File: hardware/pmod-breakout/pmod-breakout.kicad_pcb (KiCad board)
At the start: 2 copper layers, 50 x 22.9 mm, 3 parts, among them J1 Feather, J2 PMOD, J3 PMOD

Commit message: updated board + pmod
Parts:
- added REF**: Josh Details, josh-footprints:JoshDetails, B.Cu at (111.8, 65.3)
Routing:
- added copper zone on F.Cu, net GND
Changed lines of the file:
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@@
     (tracks 79)
     (zones 0)
-    (modules 3)
+    (modules 4)
     (nets 19)
   )
@@
     (last_trace_width 0.25)
     (trace_clearance 0.2)
-    (zone_clearance 0.508)
+    (zone_clearance 0.2)
     (zone_45_only no)
     (trace_min 0.2)
@@
     (solder_mask_min_width 0.25)
     (aux_axis_origin 0 0)
-    (visible_elements FFFFFF7F)
+    (visible_elements 7FFFFFFF)
     (pcbplotparams
       (layerselection 0x010fc_ffffffff)
@@
     (add_net /P2_9)
     (add_net GND)
-    (add_net "Net-(J1-Pad1)")
-    (add_net "Net-(J1-Pad13)")
-    (add_net "Net-(J1-Pad14)")
-    (add_net "Net-(J1-Pad15)")
-    (add_net "Net-(J1-Pad25)")
-    (add_net "Net-(J1-Pad26)")
-    (add_net "Net-(J1-Pad27)")
-    (add_net "Net-(J1-Pad28)")
-    (add_net "Net-(J1-Pad3)")
+  )
+  (module josh-footprints:JoshDetails (layer B.Cu)
+    (at 111.78 65.35 180)
+    (fp_text reference REF** (at 0 5.6) (layer B.Fab)
+      (effects (font (size 1 1) (thickness 0.15)) (justify mirror))
+    )
+    (fp_text value "Josh Details" (at 0 6.6) (layer B.Fab)
+      (effects (font (size 1 1) (thickness 0.15)) (justify mirror))
+    )
+    (fp_text user github.com/joshajohnson/iCE40-fpga (at 9.69 -2.19) (layer B.SilkS)
+      (effects (font (size 1 1) (thickness 0.15)) (justify mirror))
+    )
+    (fp_text user joshajohnson.com (at 2 -0.5) (layer B.SilkS)
+      (effects (font (size 1 1) (thickness 0.15)) (justify mirror))
+    )
+    (fp_text user "Josh Johnson" (at 0.2 1 180) (layer B.SilkS)
+      (effects (font (size 1 1) (thickness 0.15)) (justify mirror))
+    )
   )
   (module josh-footprints:PMOD_HOST locked (layer F.Cu)
@@
       )
     )
+  )
+  (zone (net 2) (net_name GND) (layer F.Cu) (hatch edge 0.508)
+    (connect_pads (clearance 0.2))
+    (min_thickness 0.2)
+    (fill yes (arc_segments 32) (thermal_gap 0.21) (thermal_bridge_width 0.21))
+    (polygon
+      (pts
+        (xy 85.66 57.36) (xy 135.885 57.321986) (xy 135.935 80.398013) (xy 85.71 80.436027)
+      )
+    )

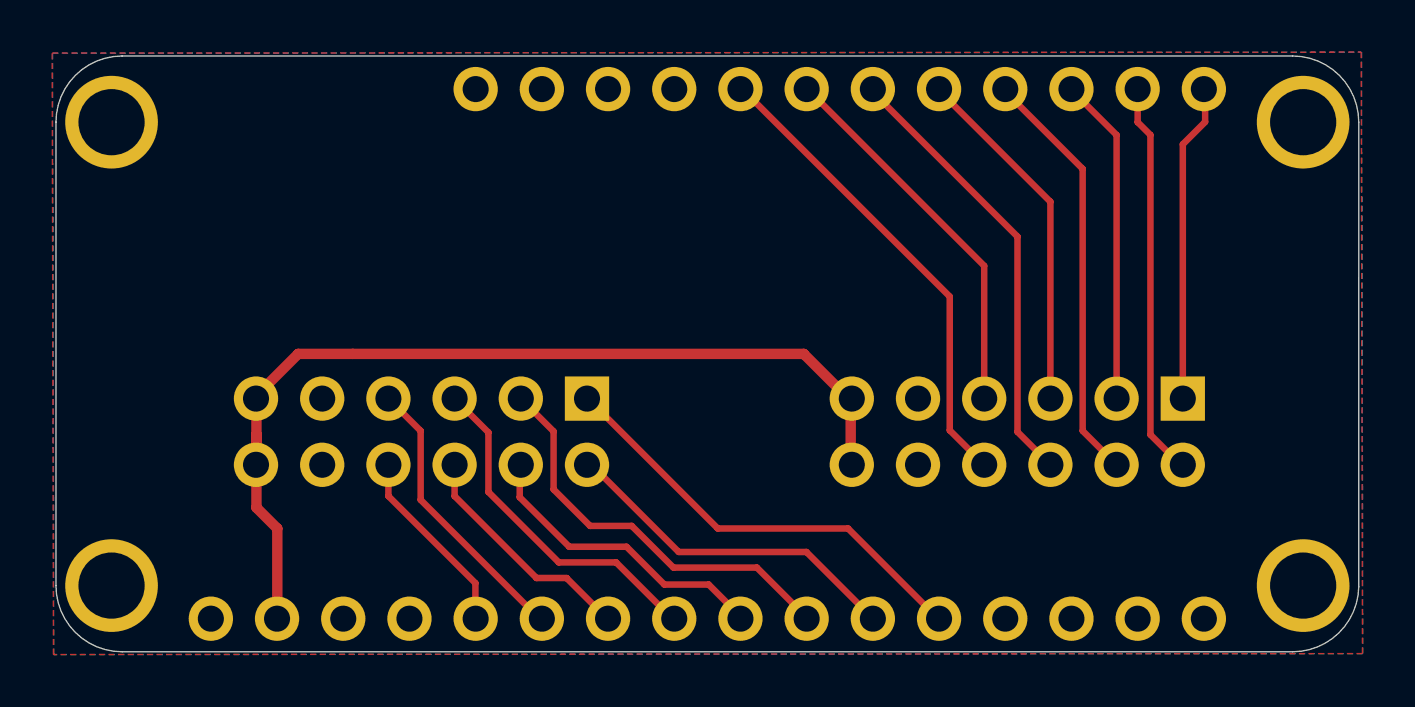
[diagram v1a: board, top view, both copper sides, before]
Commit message: changes to make everything work with new library setup
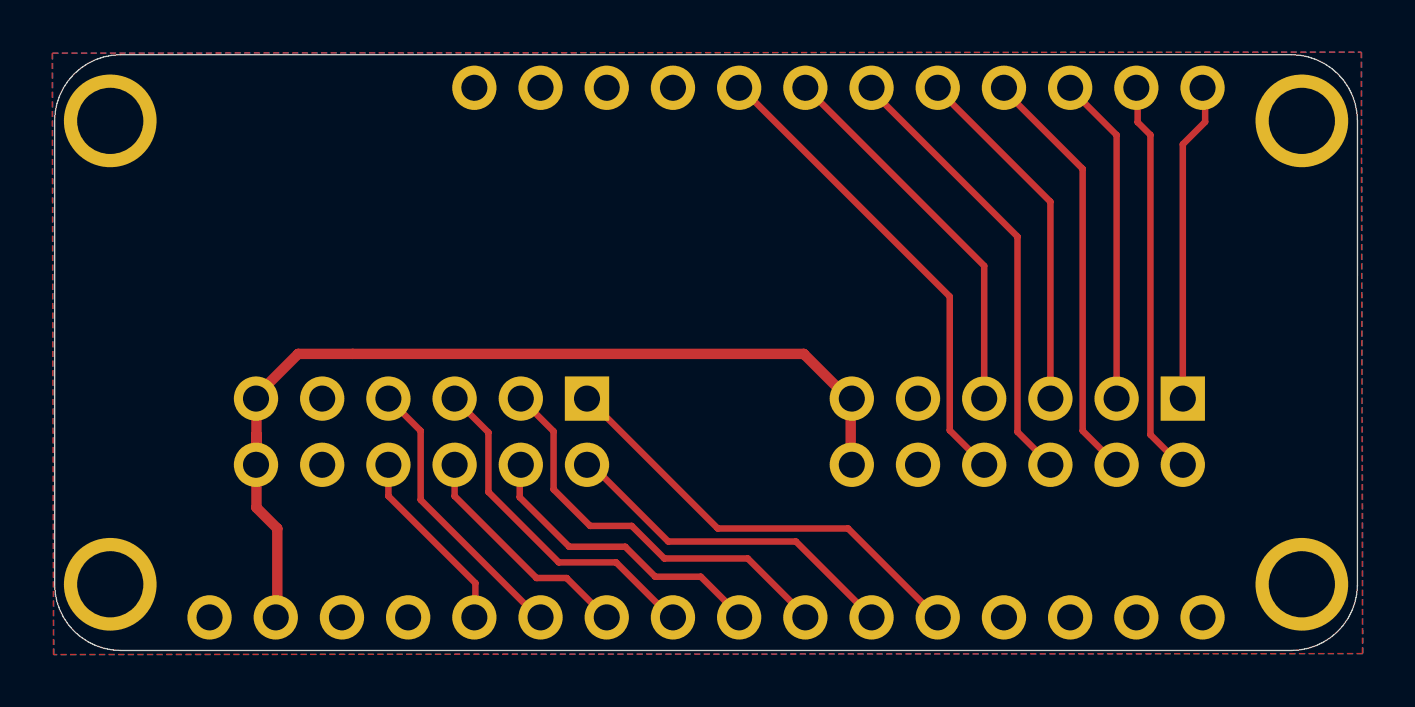
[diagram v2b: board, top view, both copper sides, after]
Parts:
- removed the REF** at (111.8, 65.3)
- added REF**: Josh Details, josh-logos:josh-details, B.Cu at (126.1, 65.6)
- J1: footprint josh-footprints:PCB_FeatherWing -> josh-connectors:featherwing
- J2, J3: footprint josh-footprints:PMOD_HOST -> josh-connectors:PMOD_HOST
- moved J1 0.07 mm to (110.8, 68.8)
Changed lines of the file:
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@@
     (add_net GND)
   )
-  (module josh-footprints:JoshDetails (layer B.Cu)
-    (at 111.78 65.35 180)
+  (module josh-logos:josh-details (layer B.Cu)
+    (at 126.1 65.6 180)
     (fp_text reference REF** (at 0 5.6) (layer B.Fab)
       (effects (font (size 1 1) (thickness 0.15)) (justify mirror))
@@
       (effects (font (size 1 1) (thickness 0.15)) (justify mirror))
     )
-    (fp_text user github.com/joshajohnson/iCE40-fpga (at 9.69 -2.19) (layer B.SilkS)
+    (fp_text user github.com/joshajohnson (at 4.6736 -2.032) (layer B.SilkS)
       (effects (font (size 1 1) (thickness 0.15)) (justify mirror))
     )
@@
     )
   )
-  (module josh-footprints:PMOD_HOST locked (layer F.Cu)
+  (module josh-connectors:PMOD_HOST locked (layer F.Cu)
     (at 99.822 75.946 270)
     (descr "Through hole angled socket strip, 2x06, 2.54mm pitch, 8.51mm socket length, double cols (from Kicad 4.0.7), script generated")
@@
       (effects (font (size 1 1) (thickness 0.15)))
     )
-    (fp_text user "Board Edge" (at 5.6388 -0.3556) (layer F.Fab)
+    (fp_text user "Board Edge" (at 2.4388 -0.3556) (layer F.Fab)
       (effects (font (size 0.8 0.8) (thickness 0.1)))
     )
-    (fp_line (start 7.2136 -0.3556) (end 6.4008 0.3048) (layer F.Fab) (width 0.12))
-    (fp_line (start 6.4008 -1.1176) (end 7.2136 -0.3556) (layer F.Fab) (width 0.12))
-    (fp_line (start 7.366 8.0772) (end 7.366 -8.0264) (layer F.Fab) (width 0.12))
+    (fp_line (start 4.0136 -0.3556) (end 3.2008 0.3048) (layer F.Fab) (width 0.12))
+    (fp_line (start 3.2008 -1.1176) (end 4.0136 -0.3556) (layer F.Fab) (width 0.12))
+    (fp_line (start 4.166 8.0772) (end 4.166 -8.0264) (layer F.Fab) (width 0.12))
     (fp_line (start -7.1308 8.13956) (end 7.7192 8.13956) (layer F.CrtYd) (width 0.05))
     (fp_line (start 7.7192 8.13956) (end 7.7192 -8.11044) (layer F.CrtYd) (width 0.05))
@@
     )
   )
-  (module josh-footprints:PMOD_HOST locked (layer F.Cu)
+  (module josh-connectors:PMOD_HOST locked (layer F.Cu)
     (at 122.682 75.946 270)
     (descr "Through hole angled socket strip, 2x06, 2.54mm pitch, 8.51mm socket length, double cols (from Kicad 4.0.7), script generated")
@@
       (effects (font (size 1 1) (thickness 0.15)))
     )
-    (fp_text user "Board Edge" (at 5.6388 -0.3556) (layer F.Fab)
+    (fp_text user "Board Edge" (at 2.4388 -0.3556) (layer F.Fab)
       (effects (font (size 0.8 0.8) (thickness 0.1)))
     )
-    (fp_line (start 7.2136 -0.3556) (end 6.4008 0.3048) (layer F.Fab) (width 0.12))
-    (fp_line (start 6.4008 -1.1176) (end 7.2136 -0.3556) (layer F.Fab) (width 0.12))
-    (fp_line (start 7.366 8.0772) (end 7.366 -8.0264) (layer F.Fab) (width 0.12))
+    (fp_line (start 4.0136 -0.3556) (end 3.2008 0.3048) (layer F.Fab) (width 0.12))
+    (fp_line (start 3.2008 -1.1176) (end 4.0136 -0.3556) (layer F.Fab) (width 0.12))
+    (fp_line (start 4.166 8.0772) (end 4.166 -8.0264) (layer F.Fab) (width 0.12))
     (fp_line (start -7.1308 8.13956) (end 7.7192 8.13956) (layer F.CrtYd) (width 0.05))
     (fp_line (start 7.7192 8.13956) (end 7.7192 -8.11044) (layer F.CrtYd) (width 0.05))
@@
     )
   )
-  (module josh-footprints:PCB_FeatherWing (layer F.Cu)
-    (at 110.8 68.9)
+  (module josh-connectors:featherwing (layer F.Cu)
+    (at 110.75 68.85)
     (fp_text reference J1 (at 0 1) (layer F.Fab)
       (effects (font (size 0.6 0.6) (thickness 0.1)))
@@
       (effects (font (size 0.6 0.5) (thickness 0.1)))
     )
-    (fp_text user %R (at 17.78 8.89 180) (layer Eco1.User)
+    (fp_text user %R (at 17.78 8.89 180) (layer Eco1.User) hide
       (effects (font (size 0.3 0.3) (thickness 0.03)))
     )
@@
   (segment (start 103.6 73.19764) (end 103.64244 73.1552) (width 0.25) (layer F.Cu) (net 7))
   (segment (start 103.6 73.6) (end 103.6 73.19764) (width 0.25) (layer F.Cu) (net 7))
-  (segment (start 110.85 77.75) (end 112.2 79.1) (width 0.25) (layer F.Cu) (net 7))
-  (segment (start 109.15 77.75) (end 110.85 77.75) (width 0.25) (layer F.Cu) (net 7))
-  (segment (start 107.7 76.3) (end 109.15 77.75) (width 0.25) (layer F.Cu) (net 7))
-  (segment (start 105.5 76.3) (end 107.7 76.3) (width 0.25) (layer F.Cu) (net 7))
+  (segment (start 110.55 77.45) (end 112.2 79.1) (width 0.25) (layer F.Cu) (net 7))
+  (segment (start 108.8 77.45) (end 110.55 77.45) (width 0.25) (layer F.Cu) (net 7))
+  (segment (start 107.65 76.3) (end 108.8 77.45) (width 0.25) (layer F.Cu) (net 7))
+  (segment (start 105.5 76.3) (end 107.65 76.3) (width 0.25) (layer F.Cu) (net 7))
   (segment (start 103.6 73.19764) (end 103.6 74.4) (width 0.25) (layer F.Cu) (net 7))
   (segment (start 103.6 74.4) (end 105.5 76.3) (width 0.25) (layer F.Cu) (net 7))
+  (segment (start 112.35 76.75) (end 114.6 79) (width 0.25) (layer F.Cu) (net 8))
   (segment (start 103.64244 70.6152) (end 104.9 71.87276) (width 0.25) (layer F.Cu) (net 8))
-  (segment (start 112.7 77.1) (end 114.6 79) (width 0.25) (layer F.Cu) (net 8))
   (segment (start 104.9 74.1) (end 106.3 75.5) (width 0.25) (layer F.Cu) (net 8))
   (segment (start 106.3 75.5) (end 107.9 75.5) (width 0.25) (layer F.Cu) (net 8))
-  (segment (start 107.9 75.5) (end 109.5 77.1) (width 0.25) (layer F.Cu) (net 8))
   (segment (start 104.9 71.87276) (end 104.9 74.1) (width 0.25) (layer F.Cu) (net 8))
-  (segment (start 109.5 77.1) (end 112.7 77.1) (width 0.25) (layer F.Cu) (net 8))
+  (segment (start 107.9 75.5) (end 109.15 76.75) (width 0.25) (layer F.Cu) (net 8))
+  (segment (start 109.15 76.75) (end 112.35 76.75) (width 0.25) (layer F.Cu) (net 8))
   (segment (start 106.18244 73.1552) (end 106.391611 73.1552) (width 0.25) (layer F.Cu) (net 9))
-  (segment (start 114.6 76.5) (end 117.2 79.1) (width 0.25) (layer F.Cu) (net 9))
-  (segment (start 109.7 76.5) (end 114.6 76.5) (width 0.25) (layer F.Cu) (net 9))
-  (segment (start 106.3 73.1) (end 109.7 76.5) (width 0.25) (layer F.Cu) (net 9))
+  (segment (start 114.2 76.1) (end 117.2 79.1) (width 0.25) (layer F.Cu) (net 9))
+  (segment (start 109.3 76.1) (end 114.2 76.1) (width 0.25) (layer F.Cu) (net 9))
+  (segment (start 106.3 73.1) (end 109.3 76.1) (width 0.25) (layer F.Cu) (net 9))
   (segment (start 106.2 73.1) (end 106.3 73.1) (width 0.25) (layer F.Cu) (net 9))
   (segment (start 106.18244 73.1552) (end 106.2 73.13764) (width 0.25) (layer F.Cu) (net 9))

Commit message: fixing things which broke resulting from library change
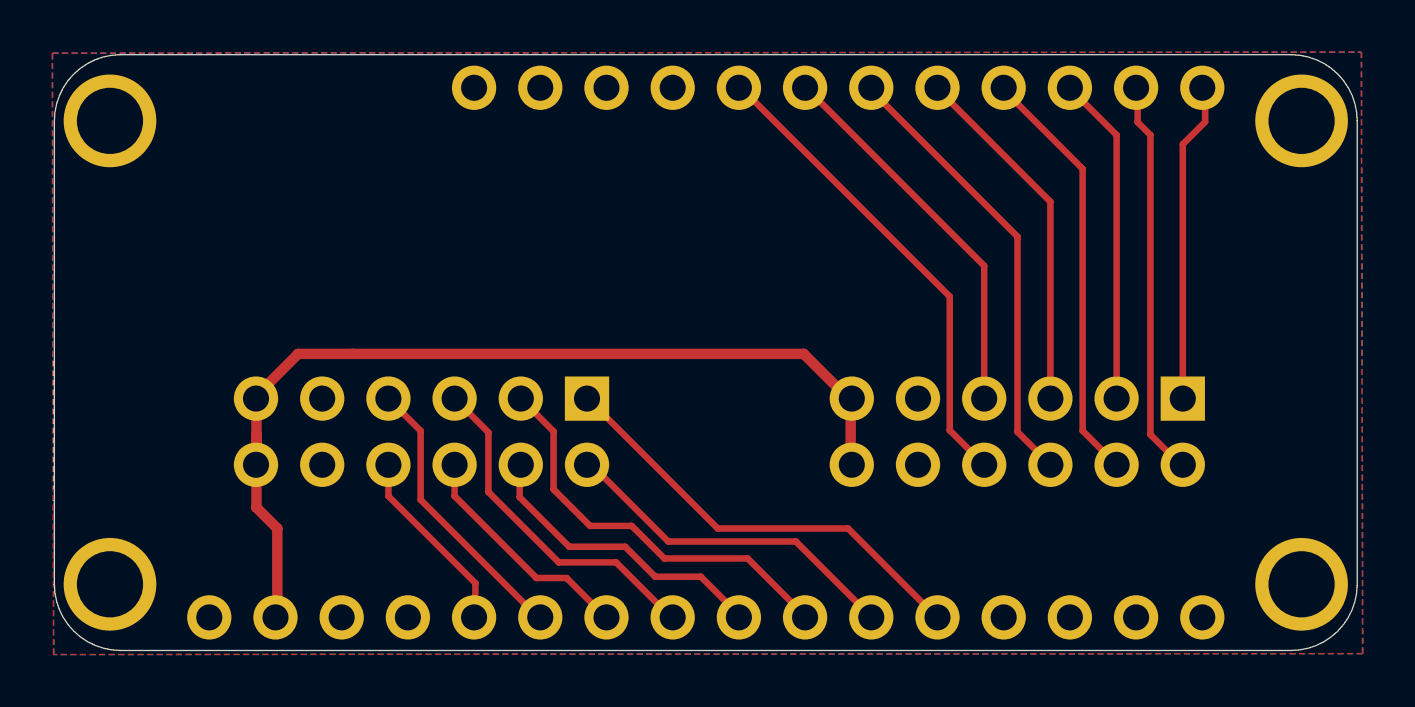
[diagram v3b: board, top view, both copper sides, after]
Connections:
- J1 pad 1: (no net) -> Net-(J1-Pad1)
- J1 pad 13: (no net) -> Net-(J1-Pad13)
- J1 pad 14: (no net) -> Net-(J1-Pad14)
- J1 pad 15: (no net) -> Net-(J1-Pad15)
- J1 pad 25: (no net) -> Net-(J1-Pad25)
- J1 pad 26: (no net) -> Net-(J1-Pad26)
- J1 pad 27: (no net) -> Net-(J1-Pad27)
- J1 pad 28: (no net) -> Net-(J1-Pad28)
- J1 pad 3: (no net) -> Net-(J1-Pad3)
